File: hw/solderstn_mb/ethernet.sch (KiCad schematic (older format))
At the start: 37 parts

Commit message: Summer vacation 2020 updates: * Front panel design rev 1 complete (incl Experimental outer board with optional linear touch sensors) * MB schematics AlmostDone(tm) - 'old' pinout supporting only one Rotary encoder * Lots of docs for new stuff
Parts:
- removed R?: 10k, symbol Device:R_Small
- added C210: 100n, symbol Device:C_Small
- gave numbers to parts that had none: 35
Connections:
- net GND: now also C210.2
- net VCC: now also C210.1
- net RMII_50M_REF_CLKO renamed RMII_REF_CLK
- net ~PHY_RESETn~ renamed ~SYS_RSTn~
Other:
- moved on the sheet: U202

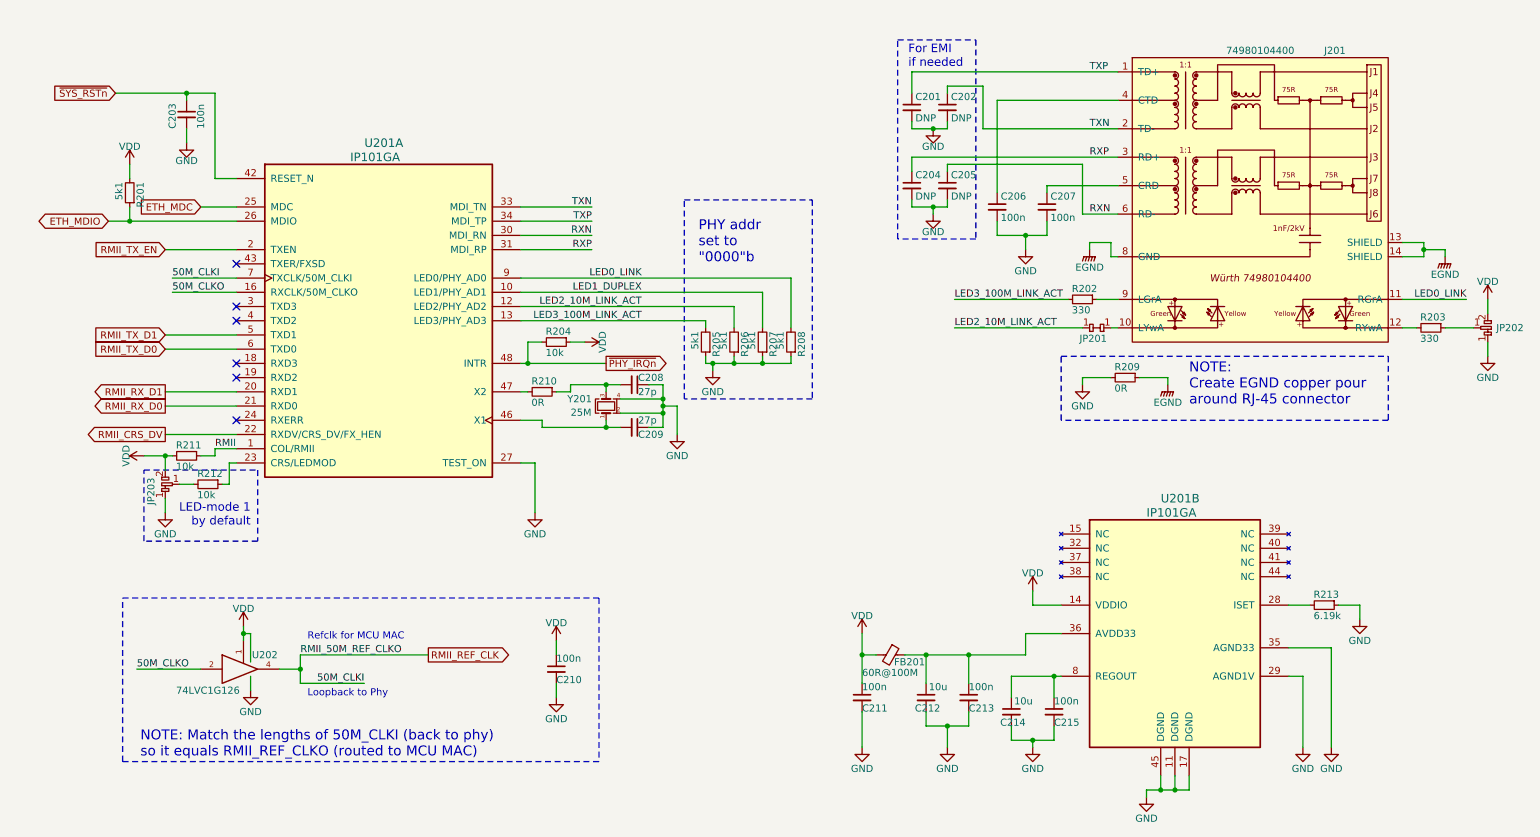
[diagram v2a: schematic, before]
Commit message: Corrected several ERC issues. Re-annotated & assigned all footprints except 32k xtal (will prob. replace with RTC module anyway)
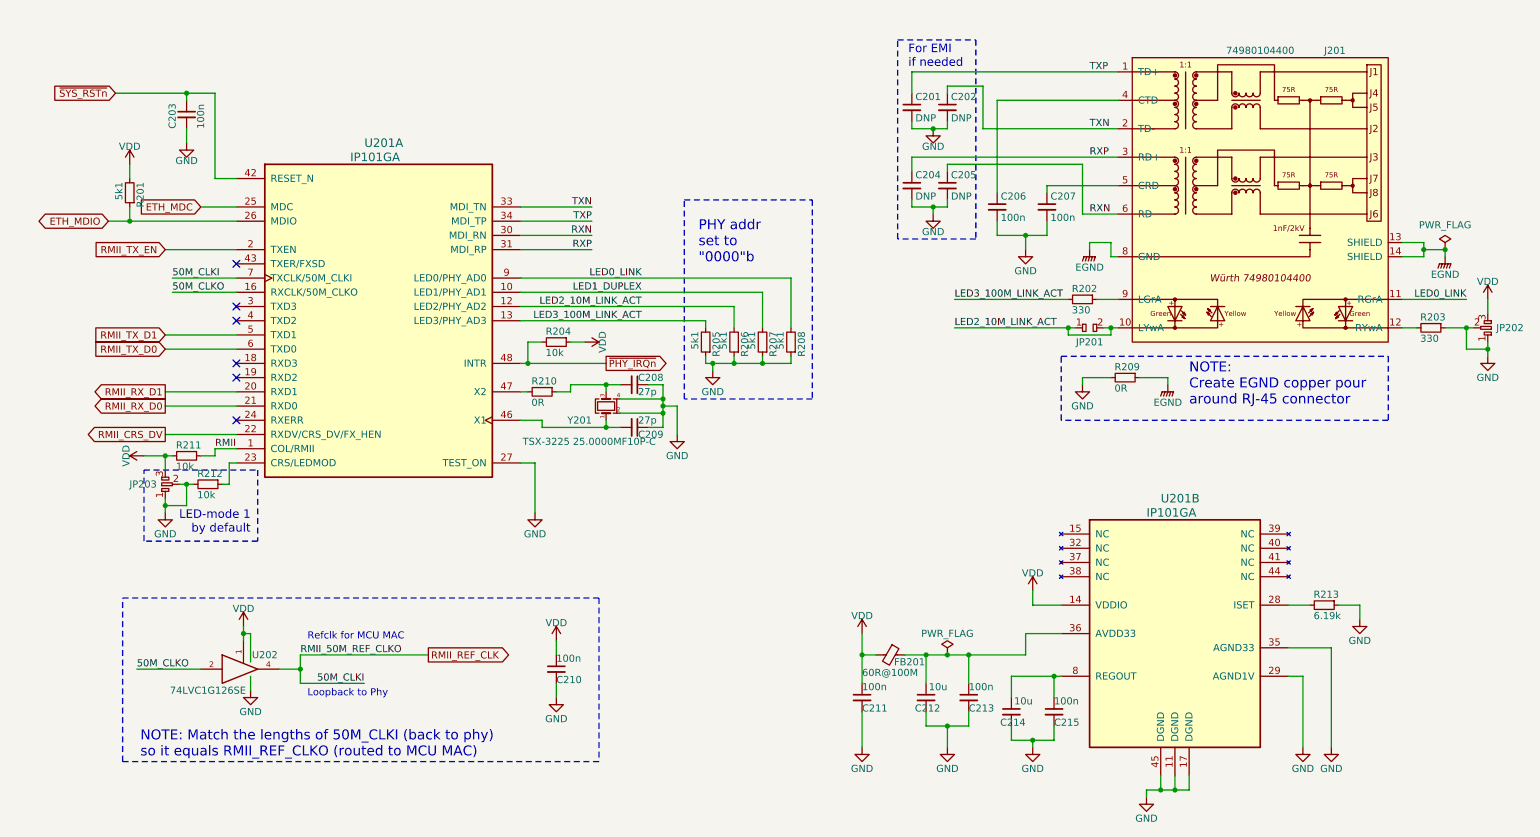
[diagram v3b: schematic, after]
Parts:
- removed JP201: dogbone_2, customlib_mj_fp:db2_0402, symbol customlib_mj:dogbone_2
- removed JP202, JP203: dogbone_3, customlib_mj_fp:db3_0402, symbol customlib_mj:dogbone_3
- added JP201: dogbone_2_ud, customlib_mj_fp:db2_ud_0402, symbol customlib_mj:dogbone_2_ud
- added JP202, JP203: dogbone_3_ud, customlib_mj_fp:db3_ud_0402, symbol customlib_mj:dogbone_3_ud
- C201, C202, C204, C205, C208, C209: footprint (none) -> Capacitor_SMD:C_0402_1005Metric
- C203, C206, C207, C210, C211, C212, C213, C214, C215: footprint (none) -> Capacitor_SMD:C_0603_1608Metric
- FB201: footprint (none) -> Inductor_SMD:L_0603_1608Metric
- J201: footprint (none) -> customlib_mj_fp:74980104400_WE-RJ45_LAN_trx
- R201, R205, R206, R207, R208, R210, R213: footprint (none) -> Resistor_SMD:R_0402_1005Metric
- R202, R203, R204, R211, R212: footprint (none) -> Resistor_SMD:R_0603_1608Metric
- U202: value 74LVC1G126 -> 74LVC1G126SE; footprint (none) -> Package_TO_SOT_SMD:SOT-353_SC-70-5_Handsoldering
- Y201: value 25M -> TSX-3225 25.0000MF10P-C; footprint Crystal:Crystal_SMD_3225-4Pin_3.2x2.5mm -> Crystal:Crystal_SMD_SeikoEpson_TSX3225-4Pin_3.2x2.5mm_HandSoldering
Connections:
- net GND: now also R203.1, R212.2, JP202.1, JP202.2, JP203.1, JP203.2
- net LED2_10M_LINK_ACT: now also J201.10 (LYwA), JP201.1, JP201.2
- net VCC: now also JP202.3, JP203.3

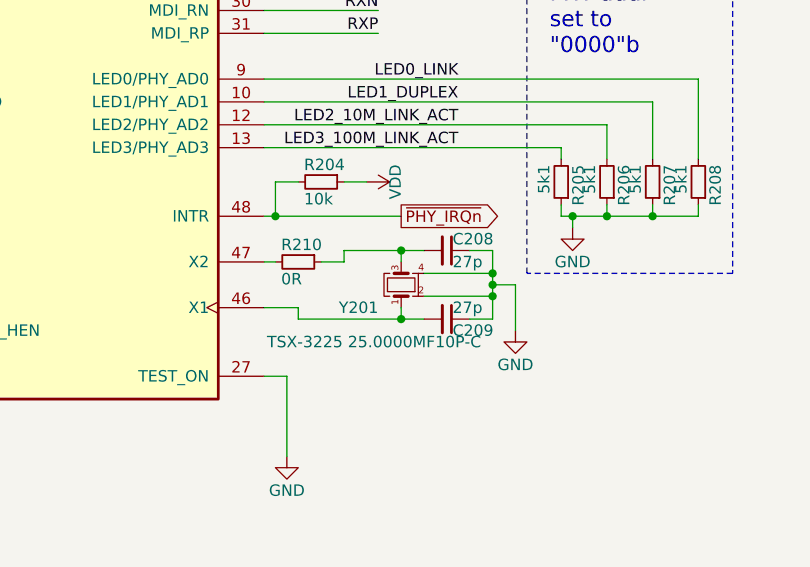
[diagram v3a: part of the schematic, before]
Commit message: Backpanel: move SMA to side, under MB PCB, also 12V-out moved outwards (and had to shift 12V/Gnd pins);   Mainboard: Move SMA-RA to bottomside, wont fit on Topside. ALso prelim. scatter/placement of some comps.
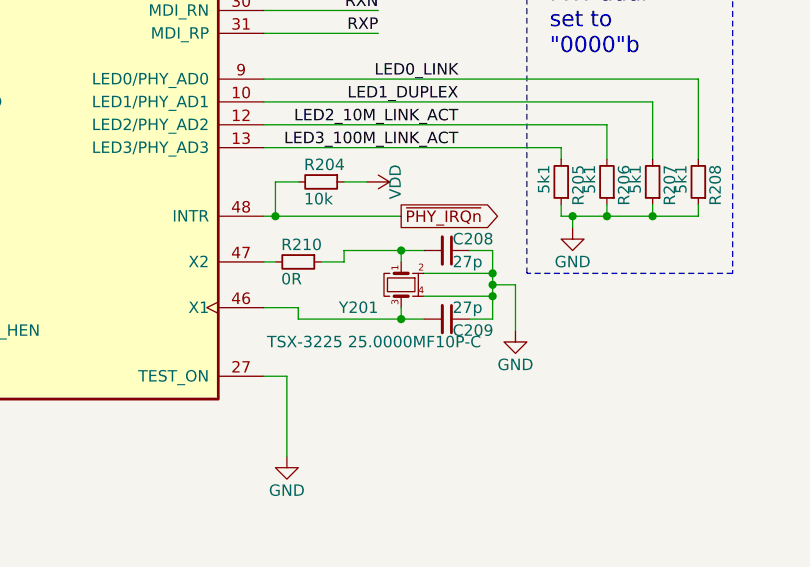
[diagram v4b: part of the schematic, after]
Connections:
- net at C209.2, U201.46 (X1): now also Y201.3; no longer Y201.1
- net at C208.2, R210.1: now also Y201.1; no longer Y201.3
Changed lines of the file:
@@
 	0    1    1    0
-$EndComp
-$Comp
-L customlib_mj:Crystal_TSX3225_25MF10P-C Y201
-U 1 1 5F3EC90A
-P 4650 3400
-F 0 "Y201" V 4550 3500 50  0000 L CNN
-F 1 "TSX-3225 25.0000MF10P-C" V 4400 3050 50  0000 L CNN
-F 2 "Crystal:Crystal_SMD_SeikoEpson_TSX3225-4Pin_3.2x2.5mm_HandSoldering" H 4650 3400 50  0001 C CNN
-F 3 "https://www.mouser.se/datasheet/2/137/FA-238_en-932914.pdf" H 4650 3400 50  0001 C CNN
-	1    4650 3400
-	0    -1   -1   0
 $EndComp
 Wire Wire Line
@@
 $EndComp
 Connection ~ 10550 2300
+$Comp
+L customlib_mj:Crystal_TSX3225_25MF10P-C Y201
+U 1 1 5F3EC90A
+P 4650 3400
+F 0 "Y201" V 4750 3500 50  0000 L CNN
+F 1 "TSX-3225 25.0000MF10P-C" V 4900 3050 50  0000 L CNN
+F 2 "Crystal:Crystal_SMD_SeikoEpson_TSX3225-4Pin_3.2x2.5mm_HandSoldering" H 4650 3400 50  0001 C CNN
+F 3 "https://www.mouser.se/datasheet/2/137/FA-238_en-932914.pdf" H 4650 3400 50  0001 C CNN
+	1    4650 3400
+	0    -1   1    0
+$EndComp
 $EndSCHEMATC

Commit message: MainBoard: change fp for all 3225 oscillators to normal (was -Handsoldering)
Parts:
- Y201: footprint Crystal:Crystal_SMD_SeikoEpson_TSX3225-4Pin_3.2x2.5mm_HandSoldering -> Crystal:Crystal_SMD_SeikoEpson_TSX3225-4Pin_3.2x2.5mm
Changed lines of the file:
@@
 F 0 "Y201" V 4750 3500 50  0000 L CNN
 F 1 "TSX-3225 25.0000MF10P-C" V 4900 3050 50  0000 L CNN
-F 2 "Crystal:Crystal_SMD_SeikoEpson_TSX3225-4Pin_3.2x2.5mm_HandSoldering" H 4650 3400 50  0001 C CNN
+F 2 "Crystal:Crystal_SMD_SeikoEpson_TSX3225-4Pin_3.2x2.5mm" H 4650 3400 50  0001 C CNN
 F 3 "https://www.mouser.se/datasheet/2/137/FA-238_en-932914.pdf" H 4650 3400 50  0001 C CNN
 	1    4650 3400

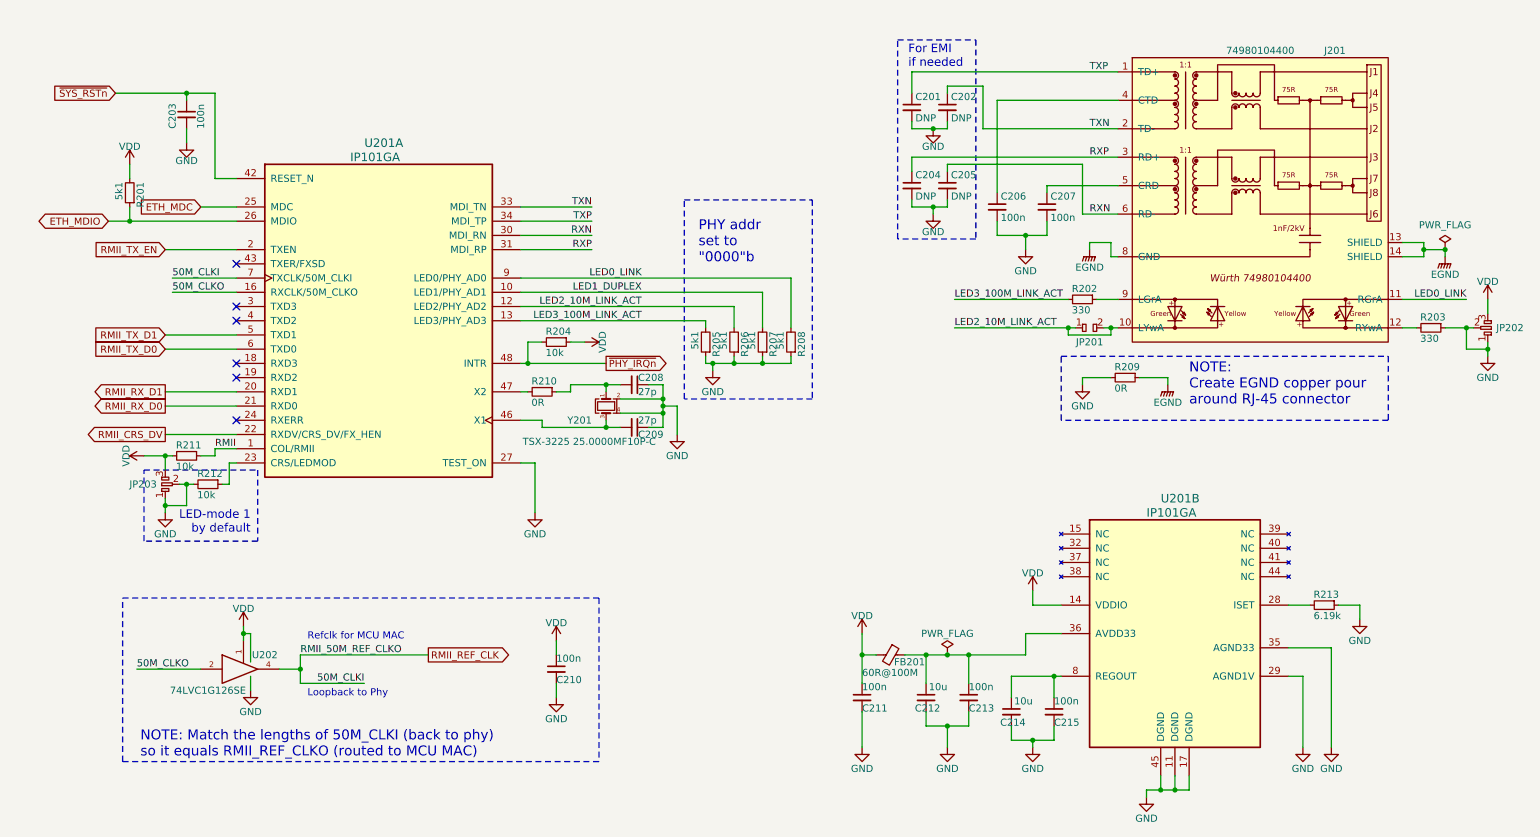
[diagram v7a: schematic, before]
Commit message: MB: major update of footprints, LCSC part numbers and Basic/Extended library indicator, for _most_ of the BoM. (Also removed JP1101/JP1102, bypass jmprs)
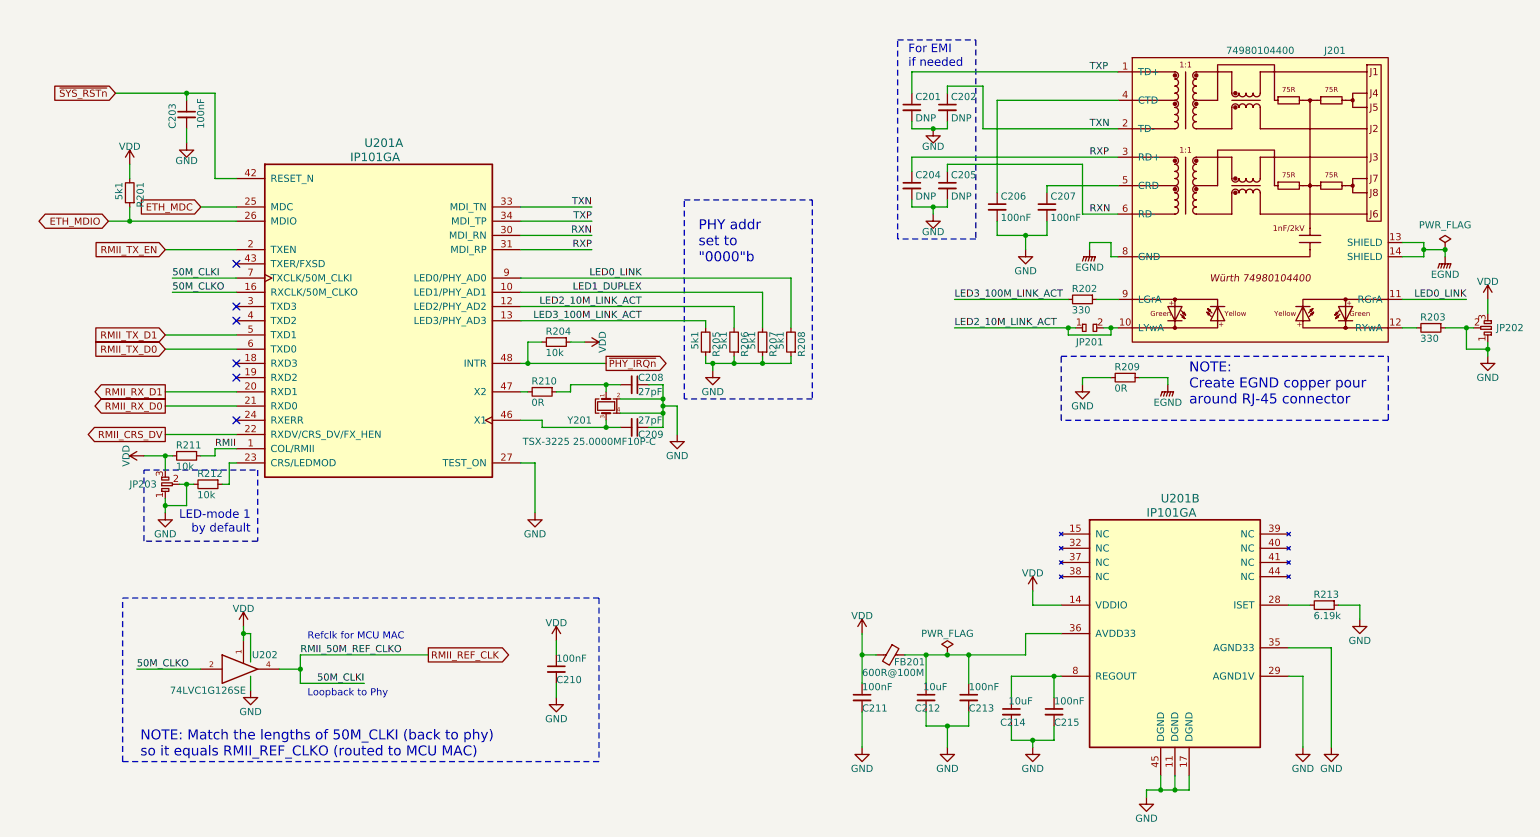
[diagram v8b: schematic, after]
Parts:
- C201, C202, C204, C205: JLC_part (none) -> Basic; LCSC (none) -> C32949
- C203, C206, C207, C210, C211, C213, C215: value 100n -> 100nF; footprint Capacitor_SMD:C_0603_1608Metric -> Capacitor_SMD:C_0402_1005Metric; JLC_part (none) -> Basic; LCSC (none) -> C1525
- C208, C209: value 27p -> 27pF; JLC_part (none) -> Basic; LCSC (none) -> C1557
- C212, C214: value 10u -> 10uF; footprint Capacitor_SMD:C_0603_1608Metric -> Capacitor_SMD:C_0402_1005Metric; JLC_part (none) -> Basic; LCSC (none) -> C15525
- FB201: value 60R@100M -> 600R@100M; JLC_part (none) -> Basic; LCSC (none) -> C1017
- R201, R205, R206, R207, R208: JLC_part (none) -> Basic; LCSC (none) -> C25905
- R202, R203: footprint Resistor_SMD:R_0603_1608Metric -> Resistor_SMD:R_0402_1005Metric; JLC_part (none) -> Basic; LCSC (none) -> C25104
- R204, R211, R212: footprint Resistor_SMD:R_0603_1608Metric -> Resistor_SMD:R_0402_1005Metric; JLC_part (none) -> Basic; LCSC (none) -> C25744
- R209: footprint Resistor_SMD:R_0603_1608Metric -> Resistor_SMD:R_0402_1005Metric; JLC_part (none) -> Basic; LCSC (none) -> C17168
- R210: JLC_part (none) -> Basic; LCSC (none) -> C17168
- R213: JLC_part (none) -> Extended; LCSC (none) -> C25914
- U201: JLC_part (none) -> Extended; LCSC (none) -> C336124
- U202: JLC_part (none) -> Extended; LCSC (none) -> C88039
- Y201: JLC_part (none) -> Basic; LCSC (none) -> C9006
